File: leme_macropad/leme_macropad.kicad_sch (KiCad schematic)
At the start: 8 parts, among them J1 USB_C_Receptacle_USB2.0_16P, J3 SWD debug, U1 NCP1117-3.3_SOT223, U2 SRV05-4HTG-D

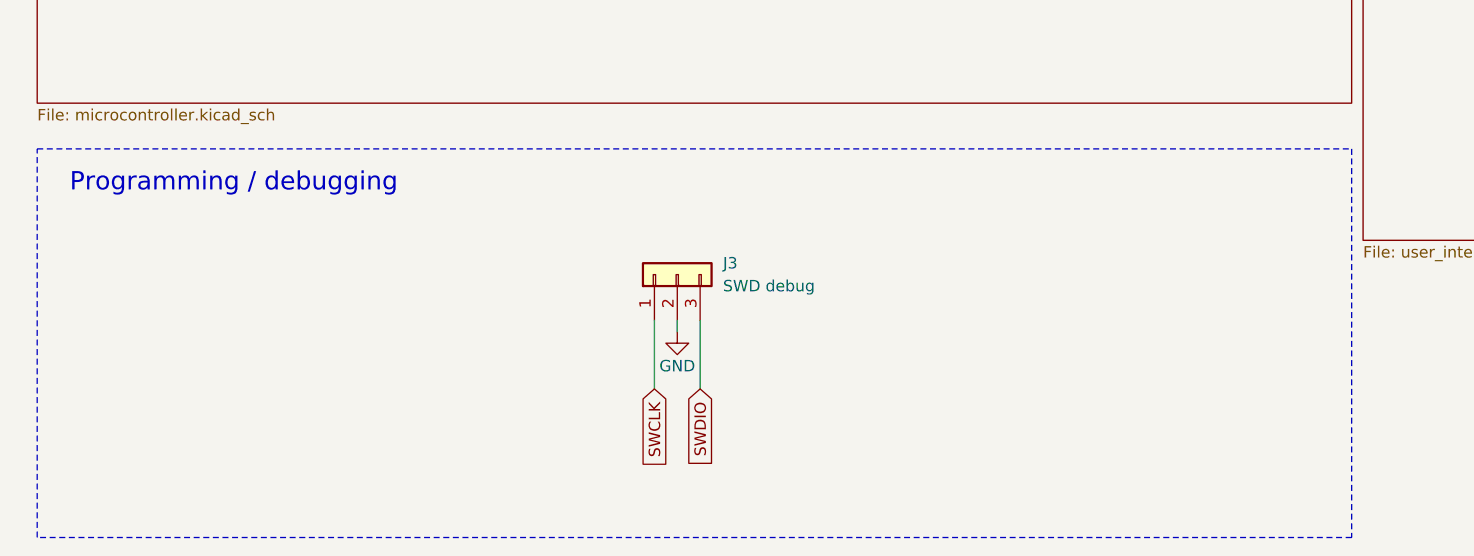
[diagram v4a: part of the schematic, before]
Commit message: Adds testpoints to a lot of signals
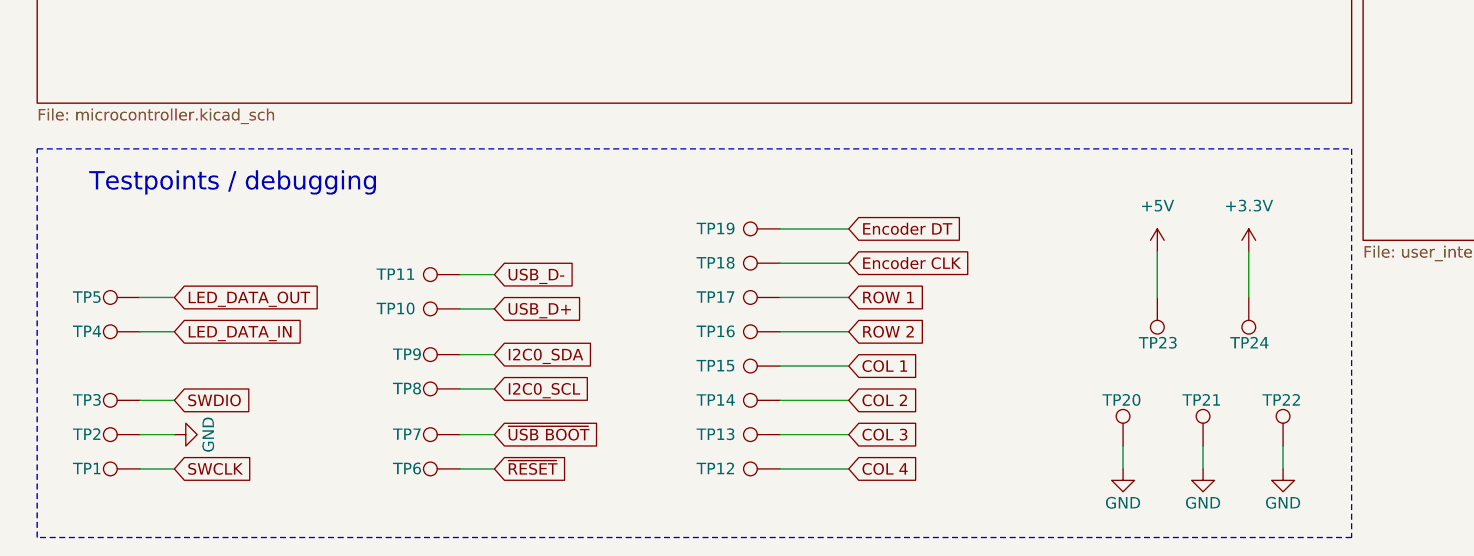
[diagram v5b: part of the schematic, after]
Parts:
- removed J3: SWD debug, symbol Connector_Generic:Conn_01x03
- added TP1, TP10, TP11, TP12, TP13, TP14, TP15, TP16, TP17, TP18, TP19, TP2, TP20, TP21, TP22, TP23, TP24, TP3, TP4, TP5, TP6, TP7, TP8, TP9: TestPoint, symbol Connector:TestPoint
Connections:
- net +3.3V: now also TP24.1
- net +5V: now also TP23.1
- net GND: now also TP2.1, TP20.1, TP21.1, TP22.1
- net SWCLK: now also TP1.1
- net SWDIO: now also TP3.1
- net USB_D+: now also TP10.1
- net USB_D-: now also TP11.1
- new net COL 1: TP15.1
- new net COL 2: TP14.1
- new net COL 3: TP13.1
- new net COL 4: TP12.1
- new net Encoder CLK: TP18.1
- new net Encoder DT: TP19.1
- new net I2C0_SCL: TP8.1
- new net I2C0_SDA: TP9.1
- new net LED_DATA_IN: TP4.1
- new net LED_DATA_OUT: TP5.1
- new net ROW 1: TP17.1
- new net ROW 2: TP16.1
- new net ~{RESET}: TP6.1
- new net ~{USB BOOT}: TP7.1
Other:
- note added: "Testpoints / debugging"
- note removed: "Programming / debugging"

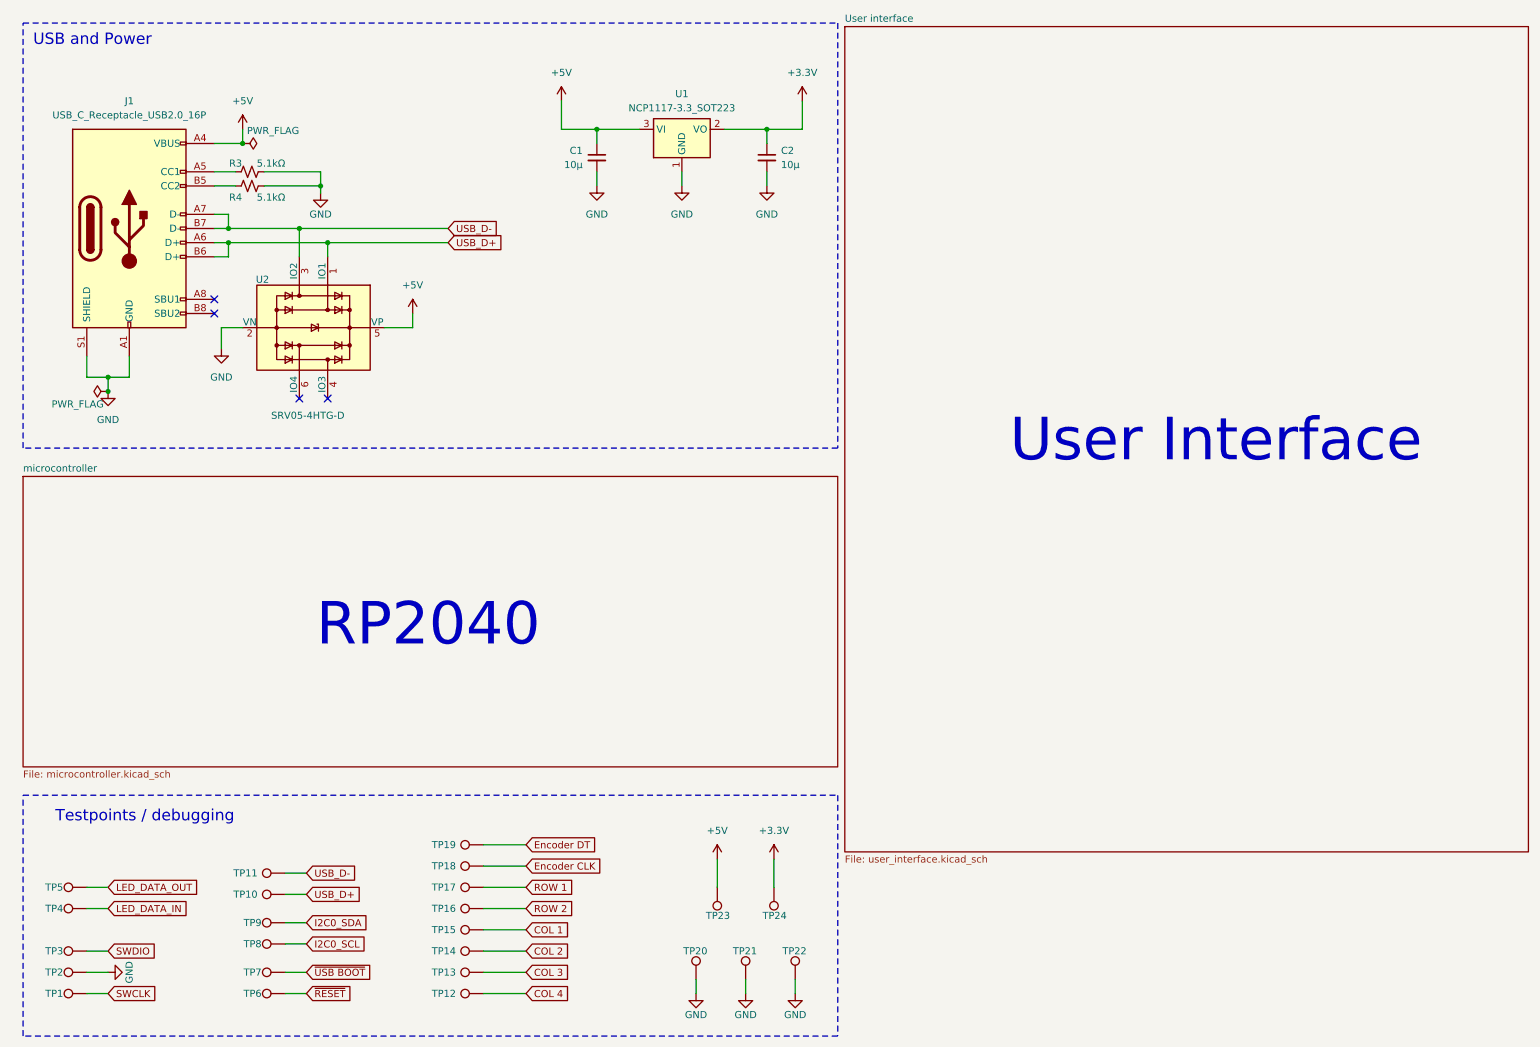
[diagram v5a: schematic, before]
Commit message: Adds testpoints to some free GPIOs
It doesn't hurt to have them broken out if we need it.
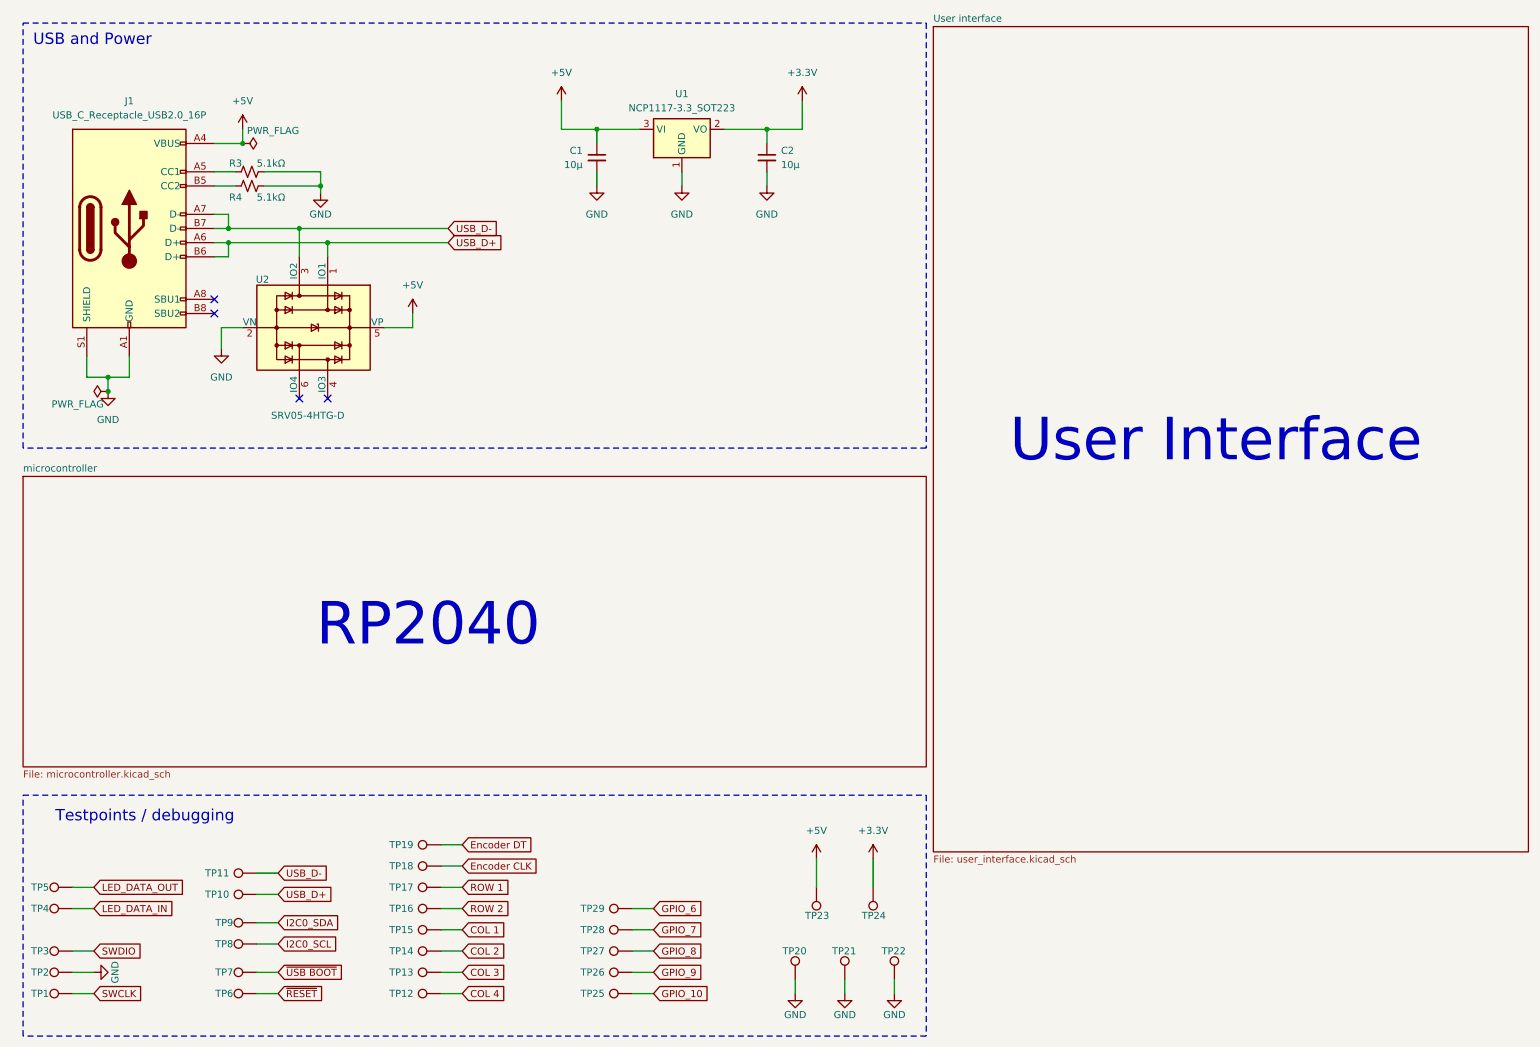
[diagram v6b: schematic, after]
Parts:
- added TP25, TP26, TP27, TP28, TP29: TestPoint, symbol Connector:TestPoint
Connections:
- new net GPIO_10: TP25.1
- new net GPIO_6: TP29.1
- new net GPIO_7: TP28.1
- new net GPIO_8: TP27.1
- new net GPIO_9: TP26.1
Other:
- moved on the sheet: TP1, TP10, TP11, TP12, TP13, TP14, TP15, TP16, TP17, TP18, TP19, TP2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

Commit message: Re-annotates schematics
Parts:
- renumbered R3 to R1, R4 to R2, TP5 to TP1, TP7 to TP10, TP6 to TP11, TP19 to TP12, TP18 to TP13, TP17 to TP14, TP16 to TP15, TP15 to TP16, TP14 to TP17, TP13 to TP18, TP12 to TP19, TP4 to TP2, TP29 to TP20, TP28 to TP21, TP27 to TP22, TP26 to TP23, TP25 to TP24, TP20 to TP25, TP23 to TP26, TP21 to TP27, TP24 to TP28, TP22 to TP29, TP2 to TP4, TP1 to TP5, TP11 to TP6, TP10 to TP7, TP9 to TP8, TP8 to TP9, U2 to U1, U1 to U2

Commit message: Reorganizes testpoints in schematics
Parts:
- renumbered TP3 to TP1, TP12 to TP10, TP13 to TP11, TP14 to TP12, TP15 to TP13, TP16 to TP14, TP17 to TP15, TP18 to TP16, TP19 to TP17, TP1 to TP18, TP2 to TP19, TP4 to TP2, TP5 to TP3, TP6 to TP4, TP7 to TP5, TP8 to TP6, TP9 to TP7, TP10 to TP8, TP11 to TP9
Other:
- moved on the sheet: TP18, TP19, TP4, TP5, TP6, TP7, TP8, TP9
